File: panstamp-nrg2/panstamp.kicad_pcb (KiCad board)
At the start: 4 copper layers, 16 x 22 mm, 28 parts, among them P1 CONN_01X10, P2 CONN_01X10, P3 CONN_01X07, P4 CONN_01X07, U1 CC430F5137, U2 BALUN+FILTER, X1 26MHz

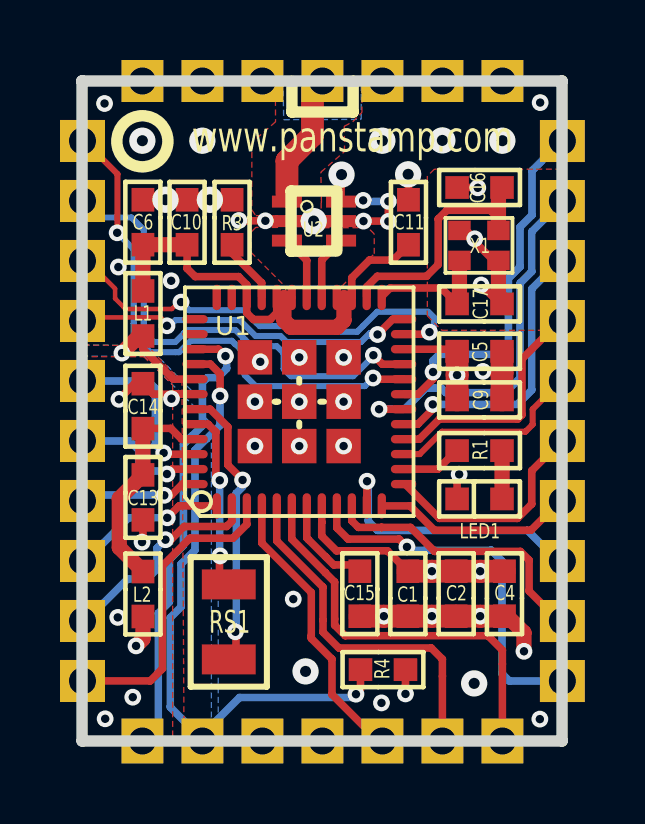
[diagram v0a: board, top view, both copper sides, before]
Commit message: Fiducials added to the PCB
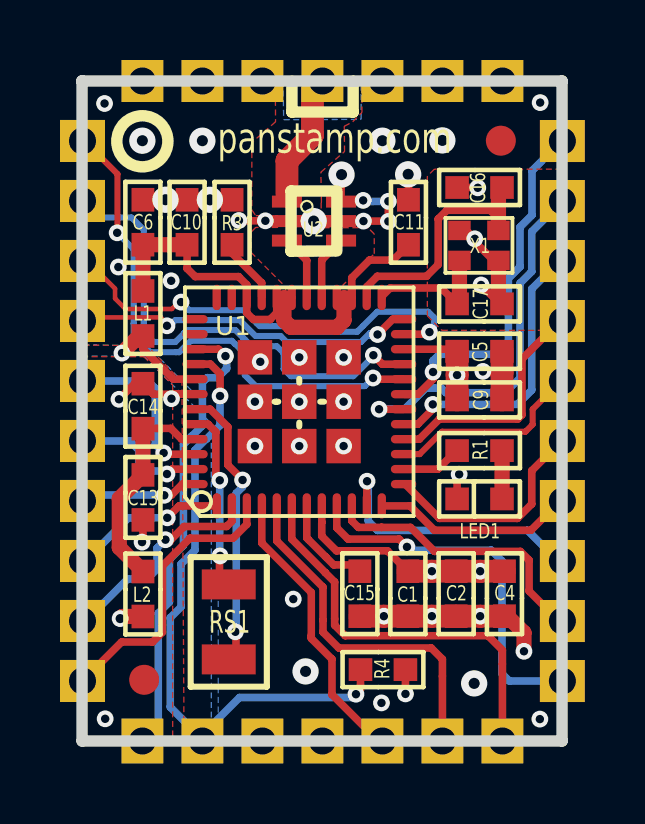
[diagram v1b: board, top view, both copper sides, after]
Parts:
- added fiducial: VAL**, mymods:fiducial, F.Cu at (170.1, 103.8)
- added fiducial: VAL**, mymods:fiducial, F.Cu at (158.2, 121.7)
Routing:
- net GND: track 74.6 -> 91.2 mm, vias 49 -> 46
- net VCC: track 35.3 -> 36.6 mm
- net /P2.0/A0: track 10.3 -> 9.55 mm
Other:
- board text added: "panstamp.com"
- board text removed: "www.panstamp.com"
